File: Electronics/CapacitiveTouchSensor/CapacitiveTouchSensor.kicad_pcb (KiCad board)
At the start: 2 copper layers, 92.7 x 104.4 mm, 151 parts, among them J1 Conn_FPCB_12

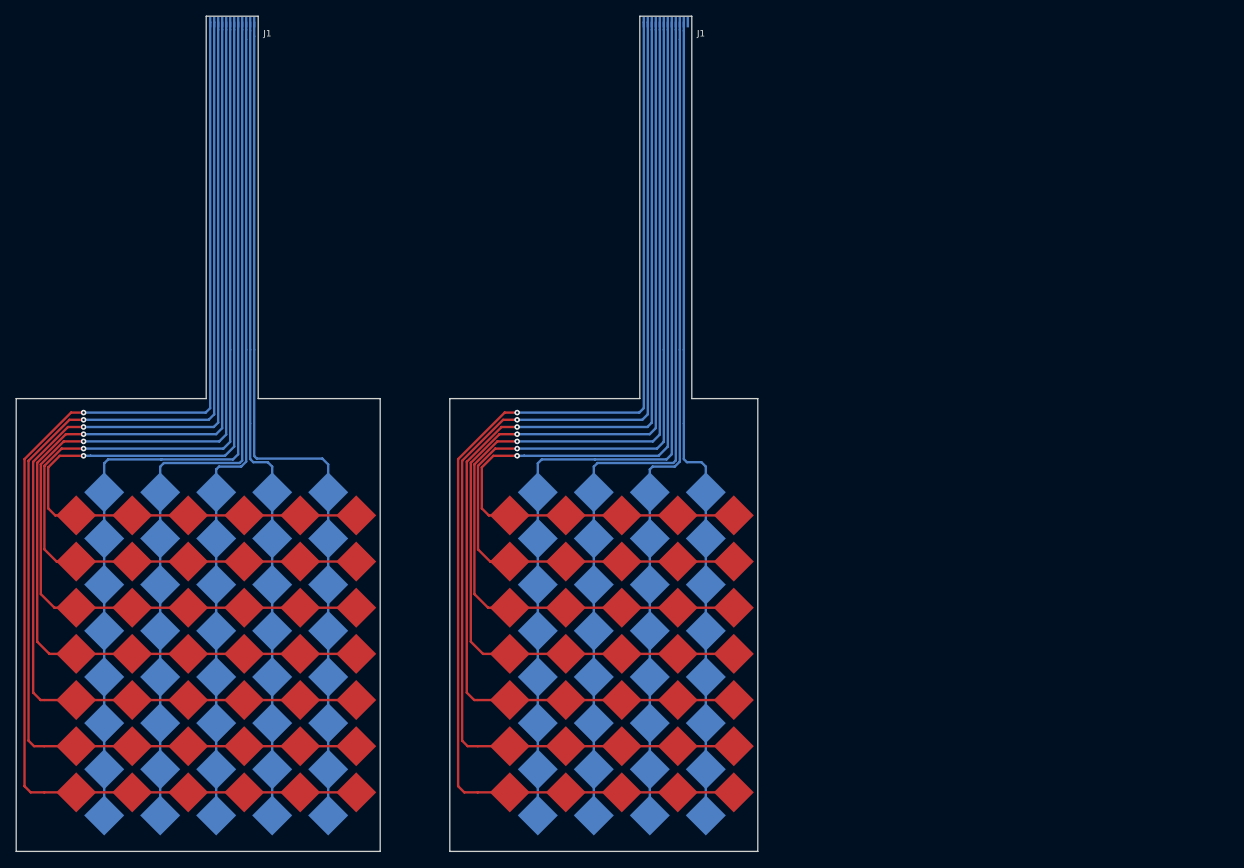
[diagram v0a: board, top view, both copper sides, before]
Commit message: feat(shielding layer): CapacitiveTouch Sensor
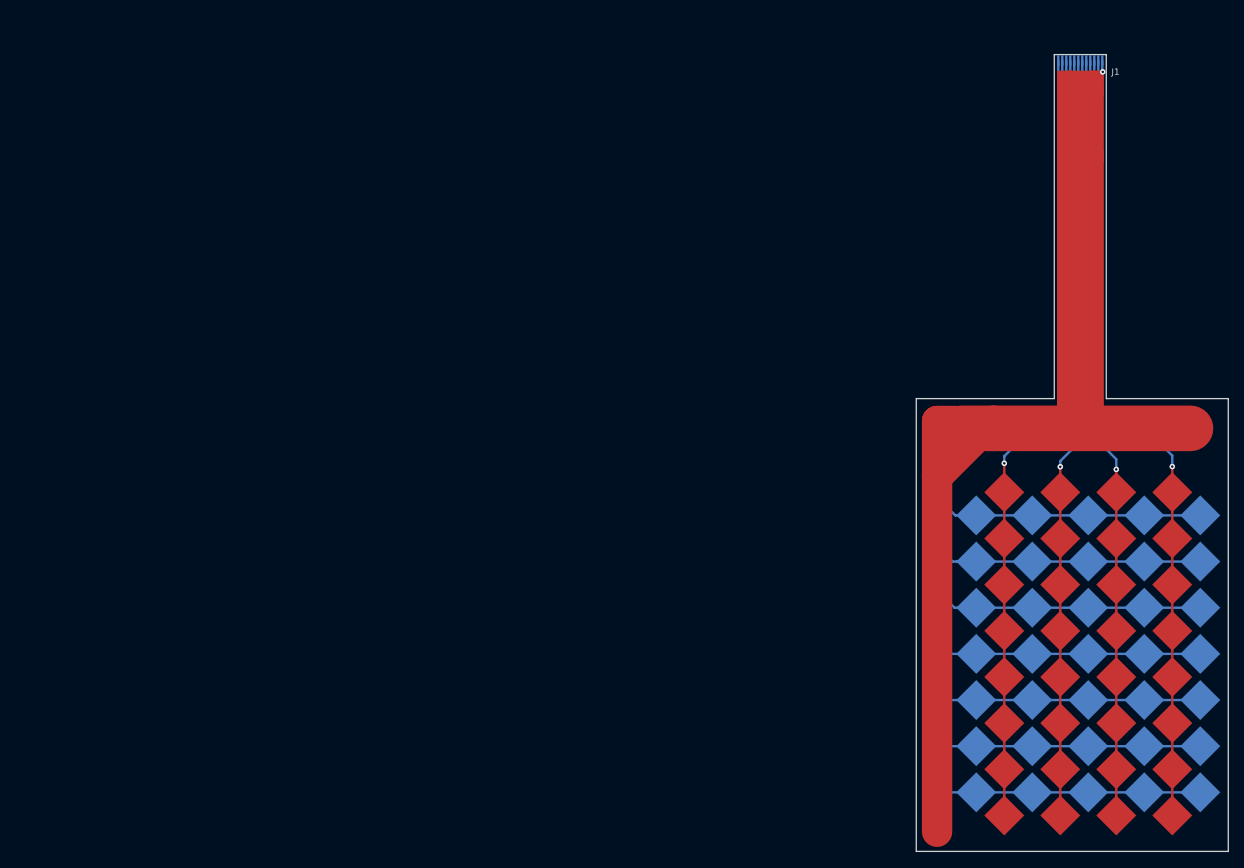
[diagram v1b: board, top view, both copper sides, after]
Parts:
- removed the D at (182.2, 134.6)
- removed the D at (175.2, 105.8)
- removed the D at (121.0, 105.8)
- removed the D at (114.0, 105.8)
- removed the D at (107.0, 105.8)
- removed the D at (124.5, 137.5)
- removed the D at (124.5, 131.7)
- removed the D at (124.5, 126.0)
- removed the D at (124.5, 120.2)
- removed the D at (124.5, 114.4)
- removed the D at (124.5, 108.7)
- removed the D at (124.5, 102.9)
- removed the D at (171.7, 102.9)
- removed the D at (117.5, 137.5)
- removed the D at (117.5, 131.7)
- removed the D at (117.5, 126.0)
- removed the D at (117.5, 120.2)
- removed the D at (117.5, 114.4)
- removed the D at (117.5, 108.7)
- removed the D at (117.5, 102.9)
- removed the D at (110.5, 137.5)
- removed the D at (110.5, 131.7)
- removed the D at (110.5, 126.0)
- removed the D at (171.7, 108.7)
- removed the D at (110.5, 120.2)
- removed the D at (110.5, 114.4)
- removed the D at (110.5, 108.7)
- removed the D at (110.5, 102.9)
- removed the D at (103.5, 137.5)
- removed the D at (103.5, 131.7)
- removed the D at (103.5, 126.0)
- removed the D at (103.5, 120.2)
- removed the D at (103.5, 114.4)
- removed the D at (103.5, 108.7)
- removed the D at (171.7, 137.5)
- removed the D at (103.5, 102.9)
- removed the D at (131.5, 137.5)
- removed the D at (131.5, 131.7)
- removed the D at (100.0, 134.6)
- removed the D at (100.0, 128.8)
- removed the D at (131.5, 126.0)
- removed the D at (131.5, 120.2)
- removed the D at (131.5, 114.4)
- removed the D at (131.5, 108.7)
- removed the D at (131.5, 102.9)
- removed the D at (171.7, 126.0)
- removed the D at (131.5, 97.1)
- removed the D at (124.5, 97.1)
- removed the D at (117.5, 97.1)
- removed the D at (110.5, 97.1)
- removed the D at (103.5, 97.1)
- removed the D at (100.0, 123.1)
- removed the D at (100.0, 117.3)
- removed the D at (100.0, 111.5)
- removed the D at (100.0, 105.8)
- removed the D at (100.0, 100.0)
- removed the D at (178.7, 137.5)
- removed the D at (182.2, 105.8)
- removed the D at (171.7, 131.7)
- removed the D at (178.7, 114.4)
- removed the D at (178.7, 120.2)
- removed the D at (168.2, 134.6)
- removed the D at (178.7, 131.7)
- removed the D at (171.7, 120.2)
- removed the D at (178.7, 108.7)
- removed the D at (168.2, 105.8)
- removed the D at (178.7, 102.9)
- removed the D at (154.2, 117.3)
- removed the D at (164.7, 97.1)
- removed the D at (154.2, 128.8)
- removed the D at (154.2, 100.0)
- removed the D at (154.2, 105.8)
- removed the D at (175.2, 128.8)
- removed the D at (157.7, 97.1)
- removed the D at (178.7, 97.1)
- removed the D at (154.2, 111.5)
- removed the D at (154.2, 123.1)
- removed the D at (171.7, 97.1)
- removed the D at (164.7, 120.2)
- removed the D at (164.7, 131.7)
- removed the D at (154.2, 134.6)
- removed the D at (157.7, 102.9)
- removed the D at (157.7, 108.7)
- removed the D at (175.2, 134.6)
- removed the D at (157.7, 114.4)
- removed the D at (157.7, 120.2)
- removed the D at (157.7, 126.0)
- removed the D at (164.7, 114.4)
- removed the D at (164.7, 108.7)
- removed the D at (157.7, 131.7)
- removed the D at (157.7, 137.5)
- removed the D at (164.7, 126.0)
- removed the D at (164.7, 137.5)
- removed the D at (164.7, 102.9)
- removed the D at (182.2, 128.8)
- removed the D at (161.2, 123.1)
- removed the D at (175.2, 123.1)
- removed the D at (175.2, 111.5)
- removed the D at (182.2, 111.5)
- removed the D at (161.2, 128.8)
- removed the D at (182.2, 123.1)
- removed the D at (161.2, 117.3)
- removed the D at (161.2, 100.0)
- removed the D at (168.2, 117.3)
- removed the D at (168.2, 100.0)
- removed the D at (161.2, 134.6)
- removed the D at (175.2, 117.3)
- removed the D at (168.2, 123.1)
- removed the D at (175.2, 100.0)
- removed the D at (182.2, 100.0)
- removed the D at (161.2, 111.5)
- removed the D at (168.2, 111.5)
- removed the D at (182.2, 117.3)
- removed the D at (168.2, 128.8)
- removed the D at (135.0, 134.6)
- removed the D at (135.0, 128.8)
- removed the D at (171.7, 114.4)
- removed the D at (135.0, 123.1)
- removed the D at (135.0, 117.3)
- removed the D at (135.0, 111.5)
- removed the D at (135.0, 105.8)
- removed the D at (135.0, 100.0)
- removed the D at (128.0, 134.6)
- removed the D at (121.0, 134.6)
- removed the D at (114.0, 134.6)
- removed the D at (107.0, 134.6)
- removed the D at (128.0, 128.8)
- removed the D at (161.2, 105.8)
- removed the D at (121.0, 128.8)
- removed the D at (114.0, 128.8)
- removed the D at (107.0, 128.8)
- removed the D at (128.0, 123.1)
- removed the D at (121.0, 123.1)
- removed the D at (114.0, 123.1)
- removed the D at (107.0, 123.1)
- removed the D at (128.0, 117.3)
- removed the D at (121.0, 117.3)
- removed the D at (114.0, 117.3)
- removed the D at (178.7, 126.0)
- removed the D at (107.0, 117.3)
- removed the D at (128.0, 111.5)
- removed the D at (121.0, 111.5)
- removed the D at (114.0, 111.5)
- removed the D at (107.0, 111.5)
- removed the D at (128.0, 100.0)
- removed the D at (121.0, 100.0)
- removed the D at (114.0, 100.0)
- removed the D at (107.0, 100.0)
- removed the D at (128.0, 105.8)
- removed the J1 at (173.7, 39.1)
- removed the J1 at (119.5, 39.1)
- added D: D, Diamond_Pattern:1_Diamond_BOTTOM, F.Cu at (212.5, 100.0)
- added D: D, Diamond_Pattern:1_Diamond_BOTTOM, F.Cu at (233.5, 100.0)
- added D: D, Diamond_Pattern:1_Diamond_BOTTOM, F.Cu at (240.5, 100.0)
- added D: D, Diamond_Pattern:1_Diamond_BOTTOM, F.Cu at (219.5, 105.8)
- added D: D, Diamond_Pattern:1_Diamond_BOTTOM, F.Cu at (226.5, 105.8)
- added D: D, Diamond_Pattern:1_Diamond_BOTTOM, F.Cu at (233.5, 105.8)
- added D: D, Diamond_Pattern:1_Diamond_BOTTOM, F.Cu at (240.5, 105.8)
- added D: D, Diamond_Pattern:1_Diamond_BOTTOM, F.Cu at (219.5, 111.5)
- added D: D, Diamond_Pattern:1_Diamond_BOTTOM, F.Cu at (226.5, 111.5)
- added D: D, Diamond_Pattern:1_Diamond_BOTTOM, F.Cu at (233.5, 111.5)
- added D: D, Diamond_Pattern:1_Diamond_BOTTOM, F.Cu at (240.5, 111.5)
- added D: D, Diamond_Pattern:1_Diamond_BOTTOM, F.Cu at (212.5, 105.8)
- added D: D, Diamond_Pattern:1_Diamond_BOTTOM, F.Cu at (219.5, 123.1)
- added D: D, Diamond_Pattern:1_Diamond_BOTTOM, F.Cu at (226.5, 123.1)
- added D: D, Diamond_Pattern:1_Diamond_BOTTOM, F.Cu at (233.5, 123.1)
- added D: D, Diamond_Pattern:1_Diamond_BOTTOM, F.Cu at (240.5, 123.1)
- added D: D, Diamond_Pattern:1_Diamond_BOTTOM, F.Cu at (219.5, 128.8)
- added D: D, Diamond_Pattern:1_Diamond_BOTTOM, F.Cu at (226.5, 128.8)
- added D: D, Diamond_Pattern:1_Diamond_BOTTOM, F.Cu at (233.5, 128.8)
- added D: D, Diamond_Pattern:1_Diamond_BOTTOM, F.Cu at (240.5, 128.8)
- added D: D, Diamond_Pattern:1_Diamond_BOTTOM, F.Cu at (219.5, 117.3)
- added D: D, Diamond_Pattern:1_Diamond_BOTTOM, F.Cu at (226.5, 117.3)
- added D: D, Diamond_Pattern:1_Diamond_BOTTOM, F.Cu at (212.5, 111.5)
- added D: D, Diamond_Pattern:1_Diamond_BOTTOM, F.Cu at (233.5, 117.3)
- added D: D, Diamond_Pattern:1_Diamond_BOTTOM, F.Cu at (240.5, 117.3)
- added D: D, Diamond_Pattern:1_Diamond_BOTTOM, F.Cu at (219.5, 134.6)
- added D: D, Diamond_Pattern:1_Diamond_BOTTOM, F.Cu at (226.5, 134.6)
- added D: D, Diamond_Pattern:1_Diamond_BOTTOM, F.Cu at (233.5, 134.6)
- added D: D, Diamond_Pattern:1_Diamond_BOTTOM, F.Cu at (240.5, 134.6)
- added D: D, Diamond_Pattern:1_Diamond_TOP, F.Cu at (216.0, 97.1)
- added D: D, Diamond_Pattern:1_Diamond_TOP, F.Cu at (223.0, 97.1)
- added D: D, Diamond_Pattern:1_Diamond_TOP, F.Cu at (230.0, 97.1)
- added D: D, Diamond_Pattern:1_Diamond_TOP, F.Cu at (237.0, 97.1)
- added D: D, Diamond_Pattern:1_Diamond_BOTTOM, F.Cu at (212.5, 117.3)
- added D: D, Diamond_Pattern:1_Diamond_TOP, F.Cu at (216.0, 102.9)
- added D: D, Diamond_Pattern:1_Diamond_TOP, F.Cu at (216.0, 108.7)
- added D: D, Diamond_Pattern:1_Diamond_TOP, F.Cu at (216.0, 114.4)
- added D: D, Diamond_Pattern:1_Diamond_TOP, F.Cu at (216.0, 120.2)
- added D: D, Diamond_Pattern:1_Diamond_TOP, F.Cu at (216.0, 126.0)
- added D: D, Diamond_Pattern:1_Diamond_TOP, F.Cu at (216.0, 131.7)
- added D: D, Diamond_Pattern:1_Diamond_TOP, F.Cu at (216.0, 137.5)
- added D: D, Diamond_Pattern:1_Diamond_TOP, F.Cu at (230.0, 102.9)
- added D: D, Diamond_Pattern:1_Diamond_TOP, F.Cu at (230.0, 108.7)
- added D: D, Diamond_Pattern:1_Diamond_TOP, F.Cu at (230.0, 114.4)
- added D: D, Diamond_Pattern:1_Diamond_BOTTOM, F.Cu at (212.5, 123.1)
- added D: D, Diamond_Pattern:1_Diamond_TOP, F.Cu at (230.0, 120.2)
- added D: D, Diamond_Pattern:1_Diamond_TOP, F.Cu at (230.0, 126.0)
- added D: D, Diamond_Pattern:1_Diamond_TOP, F.Cu at (230.0, 131.7)
- added D: D, Diamond_Pattern:1_Diamond_TOP, F.Cu at (230.0, 137.5)
- added D: D, Diamond_Pattern:1_Diamond_TOP, F.Cu at (223.0, 102.9)
- added D: D, Diamond_Pattern:1_Diamond_TOP, F.Cu at (223.0, 108.7)
- added D: D, Diamond_Pattern:1_Diamond_TOP, F.Cu at (223.0, 114.4)
- added D: D, Diamond_Pattern:1_Diamond_TOP, F.Cu at (223.0, 120.2)
- added D: D, Diamond_Pattern:1_Diamond_TOP, F.Cu at (223.0, 126.0)
- added D: D, Diamond_Pattern:1_Diamond_TOP, F.Cu at (223.0, 131.7)
- added D: D, Diamond_Pattern:1_Diamond_BOTTOM, F.Cu at (212.5, 128.8)
- added D: D, Diamond_Pattern:1_Diamond_TOP, F.Cu at (223.0, 137.5)
- added D: D, Diamond_Pattern:1_Diamond_TOP, F.Cu at (237.0, 102.9)
- added D: D, Diamond_Pattern:1_Diamond_TOP, F.Cu at (237.0, 108.7)
- added D: D, Diamond_Pattern:1_Diamond_TOP, F.Cu at (237.0, 114.4)
- added D: D, Diamond_Pattern:1_Diamond_TOP, F.Cu at (237.0, 120.2)
- added D: D, Diamond_Pattern:1_Diamond_TOP, F.Cu at (237.0, 126.0)
- added D: D, Diamond_Pattern:1_Diamond_TOP, F.Cu at (237.0, 131.7)
- added D: D, Diamond_Pattern:1_Diamond_TOP, F.Cu at (237.0, 137.5)
- added D: D, Diamond_Pattern:1_Diamond_BOTTOM, F.Cu at (212.5, 134.6)
- added D: D, Diamond_Pattern:1_Diamond_BOTTOM, F.Cu at (219.5, 100.0)
- added D: D, Diamond_Pattern:1_Diamond_BOTTOM, F.Cu at (226.5, 100.0)
- added J1: Conn_FPCB_12, Connector_FPCB:Conn_FCPB_12, F.Cu at (225.5, 43.9)
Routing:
- net (no net): track 1350.8 -> 0.00 mm, vias 7 -> 0
- net GND: track 0.00 -> 165.0 mm, vias 0 -> 1
- net 12: track 107.8 -> 0.00 mm
- net 7: track 121.1 -> 101.1 mm, vias 1 -> 0
- net 5: track 132.3 -> 113.2 mm, vias 1 -> 0
- net 4: track 138.2 -> 119.5 mm, vias 1 -> 0
- net 3: track 144.6 -> 126.1 mm, vias 1 -> 0
- net 1: track 156.5 -> 138.5 mm, vias 1 -> 0
- net 2: track 150.6 -> 132.7 mm, vias 1 -> 0
- net 6: track 126.7 -> 109.7 mm, vias 1 -> 0
- net 9: track 109.0 -> 95.9 mm, vias 0 -> 1
- net 8: track 115.2 -> 102.6 mm, vias 0 -> 1
- net 10: track 102.3 -> 95.7 mm, vias 0 -> 1
- net 11: track 101.4 -> 102.0 mm, vias 0 -> 1
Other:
- board size 92.7 x 104.4 mm -> 39 x 99.6 mm
- net class Default: clearance 0.1 -> 0.2
- rule trace_clearance: 0.1 -> 0.2
